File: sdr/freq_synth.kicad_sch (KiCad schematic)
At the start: 14 parts, among them U2 MS5351M, Y1 25MHz

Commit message: Complete layout
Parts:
- TP1, TP2, TP3: footprint TestPoint:TestPoint_Pad_D1.0mm -> TestPoint:TestPoint_Keystone_5015_Micro-Minature
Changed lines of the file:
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@@
       (effects (font (size 1.27 1.27)) (justify left))
     )
-    (property "Footprint" "TestPoint:TestPoint_Pad_D1.0mm" (at 176.53 90.17 0)
+    (property "Footprint" "TestPoint:TestPoint_Keystone_5015_Micro-Minature" (at 176.53 90.17 0)
       (effects (font (size 1.27 1.27)) hide)
     )
@@
   )
   (symbol (lib_id "Device:R") (at 177.8 90.17 90) (unit 1)
-    (in_bom yes) (on_board yes) (dnp no) (fields_autoplaced)
-    (property "Reference" "R6" (at 177.8 83.82 90)
-      (effects (font (size 1.27 1.27)))
-    )
-    (property "Value" "0" (at 177.8 86.36 90)
+    (in_bom yes) (on_board yes) (dnp no)
+    (property "Reference" "R6" (at 177.8307 92.1898 90)
+      (effects (font (size 1.27 1.27)))
+    )
+    (property "Value" "0" (at 177.8 90.17 90)
       (effects (font (size 1.27 1.27)))
     )
@@
       (effects (font (size 1.27 1.27)) (justify left))
     )
-    (property "Footprint" "TestPoint:TestPoint_Pad_D1.0mm" (at 173.99 95.25 0)
+    (property "Footprint" "TestPoint:TestPoint_Keystone_5015_Micro-Minature" (at 173.99 95.25 0)
       (effects (font (size 1.27 1.27)) hide)
     )
@@
       (effects (font (size 1.27 1.27)) (justify right))
     )
-    (property "Footprint" "TestPoint:TestPoint_Pad_D1.0mm" (at 161.29 100.33 0)
+    (property "Footprint" "TestPoint:TestPoint_Keystone_5015_Micro-Minature" (at 161.29 100.33 0)
       (effects (font (size 1.27 1.27)) hide)
     )
@@
   )
   (symbol (lib_id "Device:R") (at 177.8 100.33 90) (unit 1)
-    (in_bom yes) (on_board yes) (dnp no) (fields_autoplaced)
-    (property "Reference" "R8" (at 177.8 93.98 90)
-      (effects (font (size 1.27 1.27)))
-    )
-    (property "Value" "0" (at 177.8 96.52 90)
+    (in_bom yes) (on_board yes) (dnp no)
+    (property "Reference" "R8" (at 177.8 102.87 90)
+      (effects (font (size 1.27 1.27)))
+    )
+    (property "Value" "0" (at 177.8 100.33 90)
       (effects (font (size 1.27 1.27)))
     )
@@
   )
   (symbol (lib_id "Device:R") (at 177.8 95.25 90) (unit 1)
-    (in_bom yes) (on_board yes) (dnp no) (fields_autoplaced)
-    (property "Reference" "R7" (at 177.8 88.9 90)
-      (effects (font (size 1.27 1.27)))
-    )
-    (property "Value" "0" (at 177.8 91.44 90)
-      (effects (font (size 1.27 1.27)))
-    )
+    (in_bom yes) (on_board yes) (dnp no)
+    (property "Reference" "R7" (at 177.8 97.79 90)
+      (effects (font (size 1.27 1.27)))
+    )
+    (property "Value" "0" (at 177.8 95.25 90)
+      (effects (font (size 1.27 1.27)))
+    )

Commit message: First version 0.1 completed
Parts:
- C19, C20: value 2p -> 2.2p
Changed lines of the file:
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@@
   (symbol (lib_id "Device:C") (at 128.27 100.33 0) (unit 1)
     (in_bom yes) (on_board yes) (dnp no) (fields_autoplaced)
-    (property "Reference" "C20" (at 132.08 99.0599 0)
+    (property "Reference" "C20" (at 132.08 99.695 0)
       (effects (font (size 1.27 1.27)) (justify left))
     )
-    (property "Value" "2p" (at 132.08 101.5999 0)
+    (property "Value" "2.2p" (at 132.08 102.235 0)
       (effects (font (size 1.27 1.27)) (justify left))
     )
@@
   (symbol (lib_id "Device:C") (at 120.65 91.44 0) (mirror x) (unit 1)
     (in_bom yes) (on_board yes) (dnp no) (fields_autoplaced)
-    (property "Reference" "C19" (at 116.84 90.1699 0)
+    (property "Reference" "C19" (at 116.84 90.805 0)
       (effects (font (size 1.27 1.27)) (justify right))
     )
-    (property "Value" "2p" (at 116.84 92.7099 0)
+    (property "Value" "2.2p" (at 116.84 93.345 0)
       (effects (font (size 1.27 1.27)) (justify right))
     )

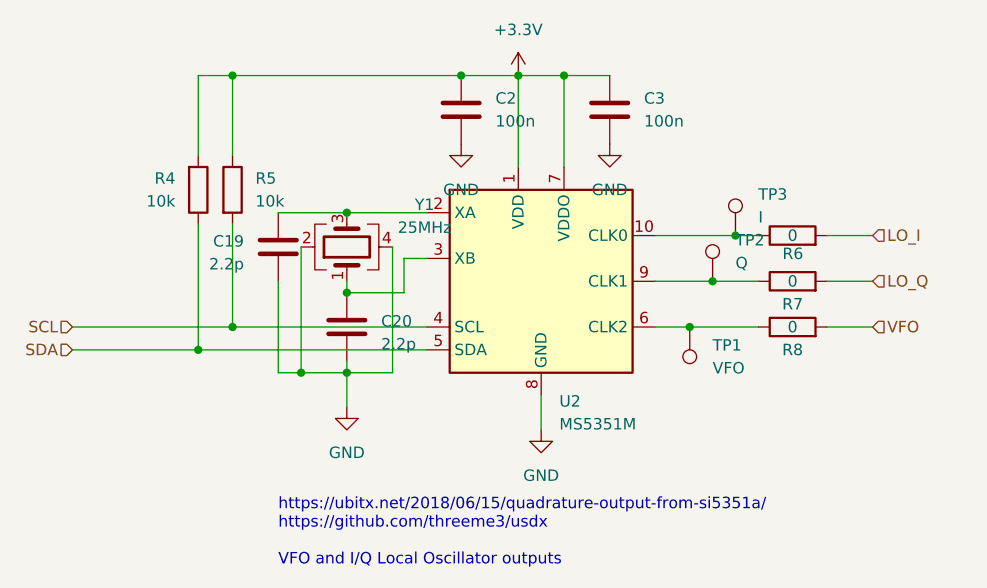
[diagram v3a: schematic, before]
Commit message: Added extra pullup resistors on the OLED i2C. Changed the Synthesizer pullups to 2.2k from 10k
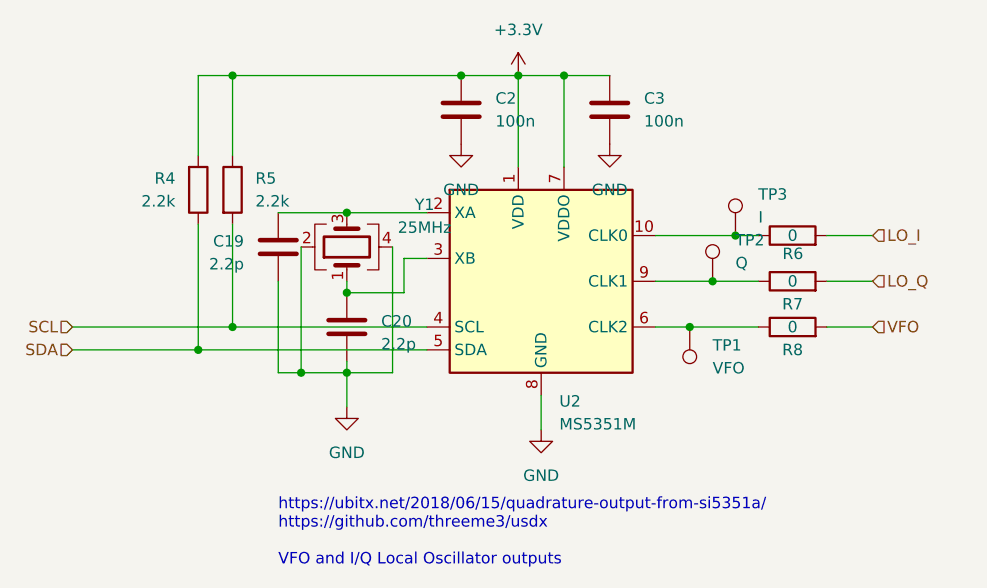
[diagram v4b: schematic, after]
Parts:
- R4, R5: value 10k -> 2.2k
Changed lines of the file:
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@@
       (effects (font (size 1.27 1.27)) (justify right))
     )
-    (property "Value" "10k" (at 109.22 86.3599 0)
+    (property "Value" "2.2k" (at 109.22 86.3599 0)
       (effects (font (size 1.27 1.27)) (justify right))
     )
@@
       (effects (font (size 1.27 1.27)) (justify left))
     )
-    (property "Value" "10k" (at 118.11 86.3599 0)
-      (effects (font (size 1.27 1.27)) (justify left))
-    )
+    (property "Value" "2.2k" (at 118.11 86.3599 0)
+      (effects (font (size 1.27 1.27)) (justify left))
+    )
